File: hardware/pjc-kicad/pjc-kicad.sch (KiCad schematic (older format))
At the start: 90 parts

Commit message: More work on Hardware section of Developers Guide.
Also added 1k resistor and 100nF cap to USB Enable P-MOSFET to more closely match circuit in FT23R datasheet.
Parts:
- added C?: 100nF, symbol C
- added R?: 1k, symbol R
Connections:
- net +5V_USB: now also C?.2
- net ~USB_PWREN: now also C?.1, R?.2; no longer R?.2, U?.14 (CBUS3)
- new net: R?.1, R?.2, U?.14 (CBUS3)
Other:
- moved on the sheet: C?, CON?, L?, Q?, R?, TP?, U?

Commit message: Finished Hardware section in Dev Guide
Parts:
- gave numbers to parts that had none: 90
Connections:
- net GND: now also U10.1 (S), U8.4 (S); no longer U10.4 (S), U8.1 (S)
- net LAMP_EN: now also TP16.1, U10.5 (G); no longer R16.1, TP12.1, U8.2 (G)
- net LED_EN_GREEN: now also U10.2 (G); no longer U10.5 (G)
- net LED_EN_RED: now also R16.1, TP12.1, U8.2 (G); no longer TP16.1, U10.5 (G)
- net LED_EN_YELLOW: now also U8.5 (G); no longer U8.2 (G)
- net at U5.6 ((PCINT20/XCK/T0)PD4): now also JP1.2, R15.1
- net at CON9.2 (PM): now also U10.6 (D); no longer U10.3 (D)
- net at CON7.2 (PM): now also U8.3 (D); no longer U8.6 (D)

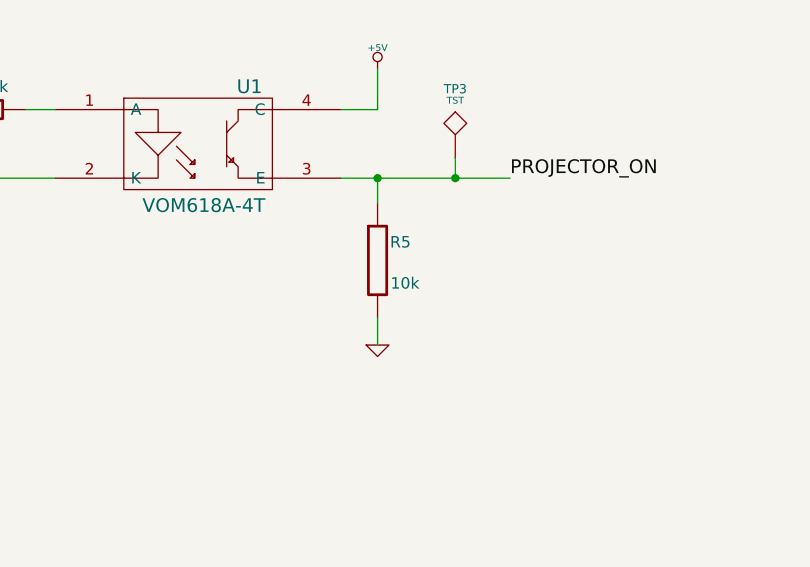
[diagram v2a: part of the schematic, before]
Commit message: More work on Firmware section of doc and put 20kOhm pulldown on opto collector to reduce the current needed to saturate it (useful for 3.3V inputs).
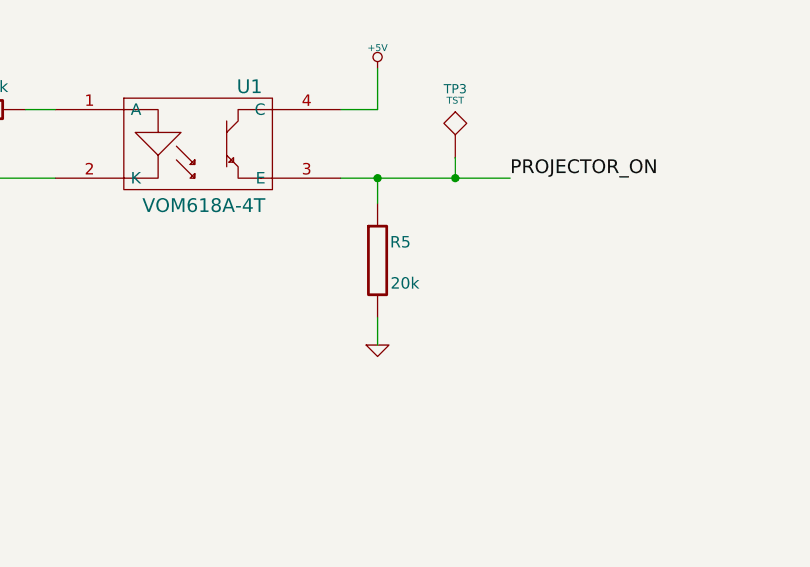
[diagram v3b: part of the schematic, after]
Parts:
- R5: value 10k -> 20k

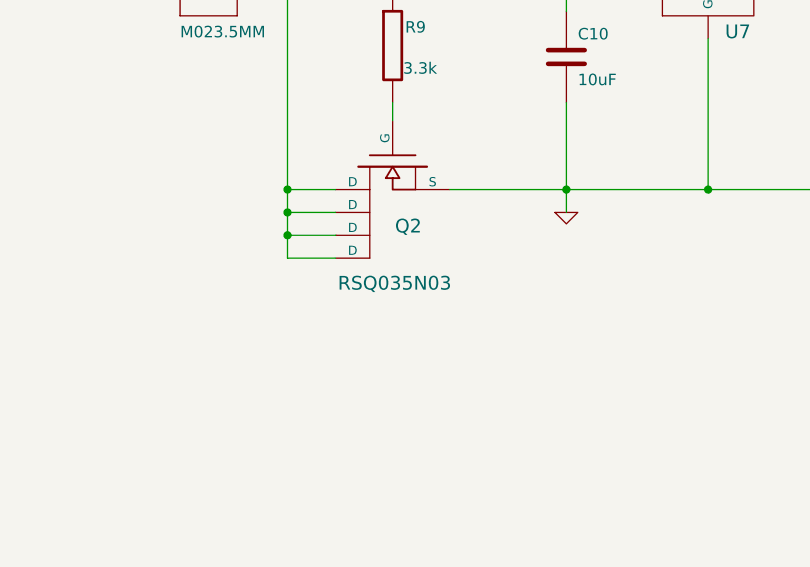
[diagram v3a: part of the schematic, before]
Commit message: Replace Rohm RSQ035N03 with RSQ045N03 since the former appears to be discontinued.  The latter has better specs anyway.
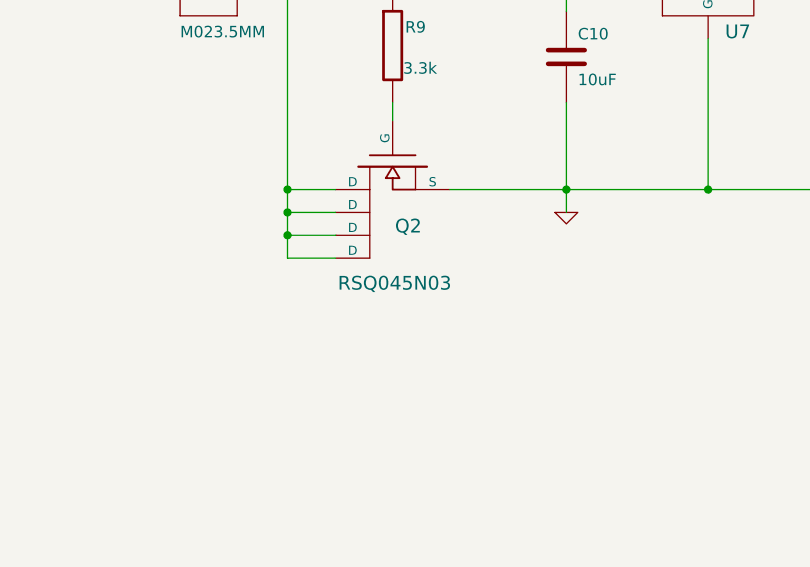
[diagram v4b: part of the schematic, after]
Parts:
- Q2: value RSQ035N03 -> RSQ045N03
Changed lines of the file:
@@
-EESchema Schematic File Version 2  date Wed 13 Feb 2013 07:00:38 PM EST
+EESchema Schematic File Version 2  date Sat 23 Feb 2013 07:02:45 PM EST
 LIBS:power
 LIBS:device
@@
 Sheet 1 1
 Title "Projector Controller Board"
-Date "13 feb 2013"
+Date "24 feb 2013"
 Rev "A"
 Comp ""
@@
 P 11090 3730
 F 0 "Q2" V 11350 3720 60  0000 R CNN
-F 1 "RSQ035N03" V 11600 3970 60  0000 R CNN
+F 1 "RSQ045N03" V 11600 3970 60  0000 R CNN
 F 2 "" H 11090 3730 60  0001 C CNN
 F 3 "" H 11090 3730 60  0001 C CNN

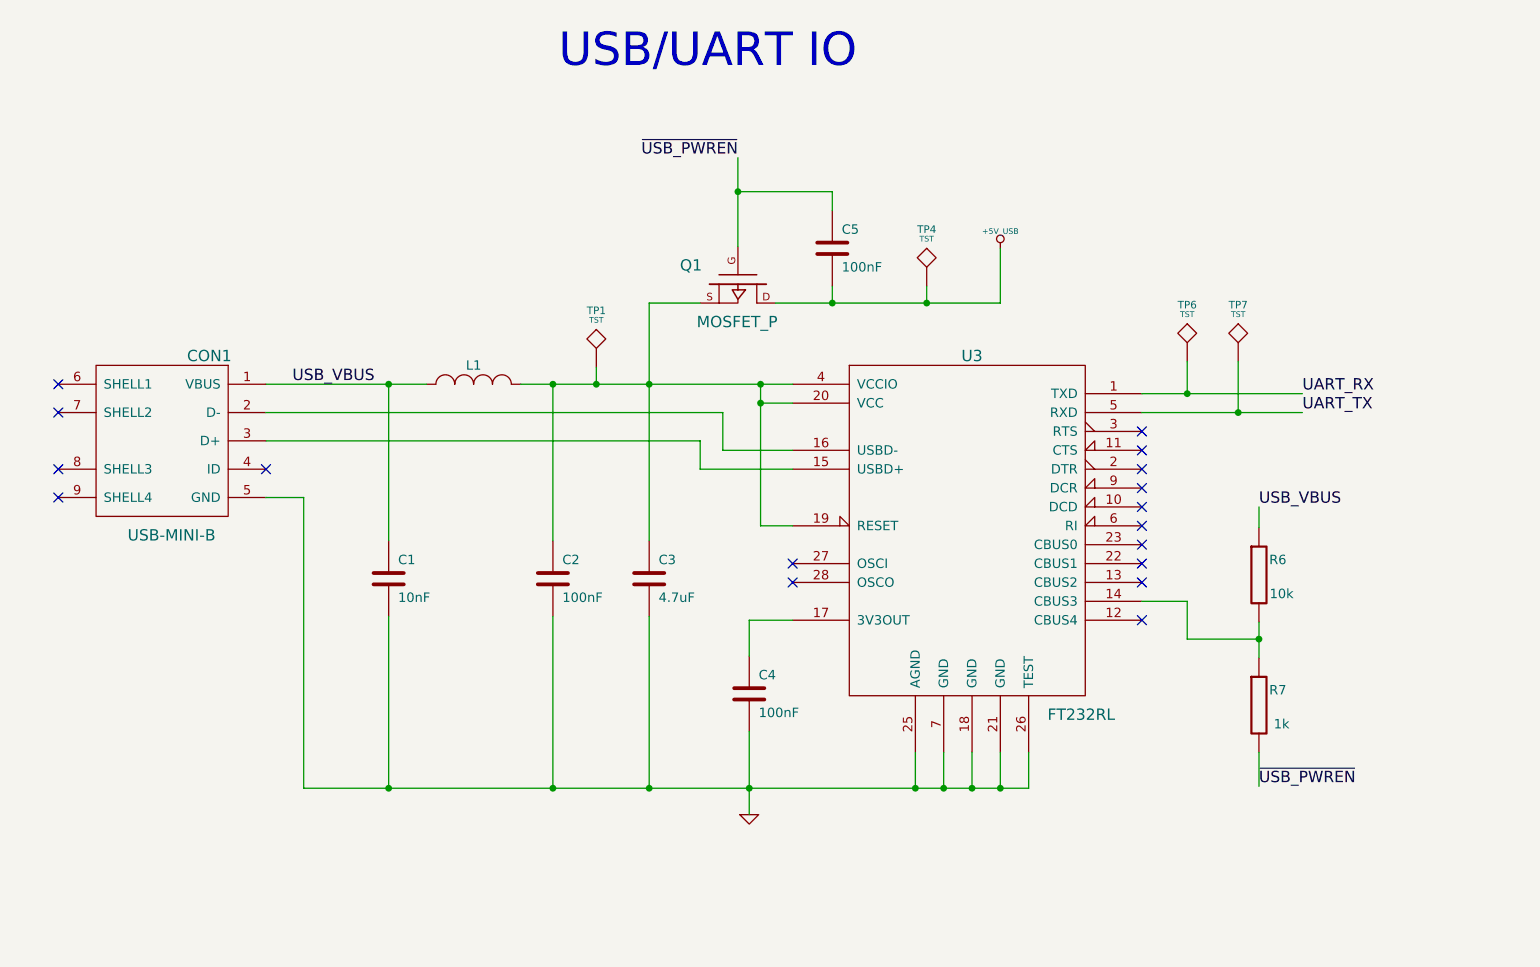
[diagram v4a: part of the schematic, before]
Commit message: Fix schematic errors found by KiCad and create symbol<-->footprint associations
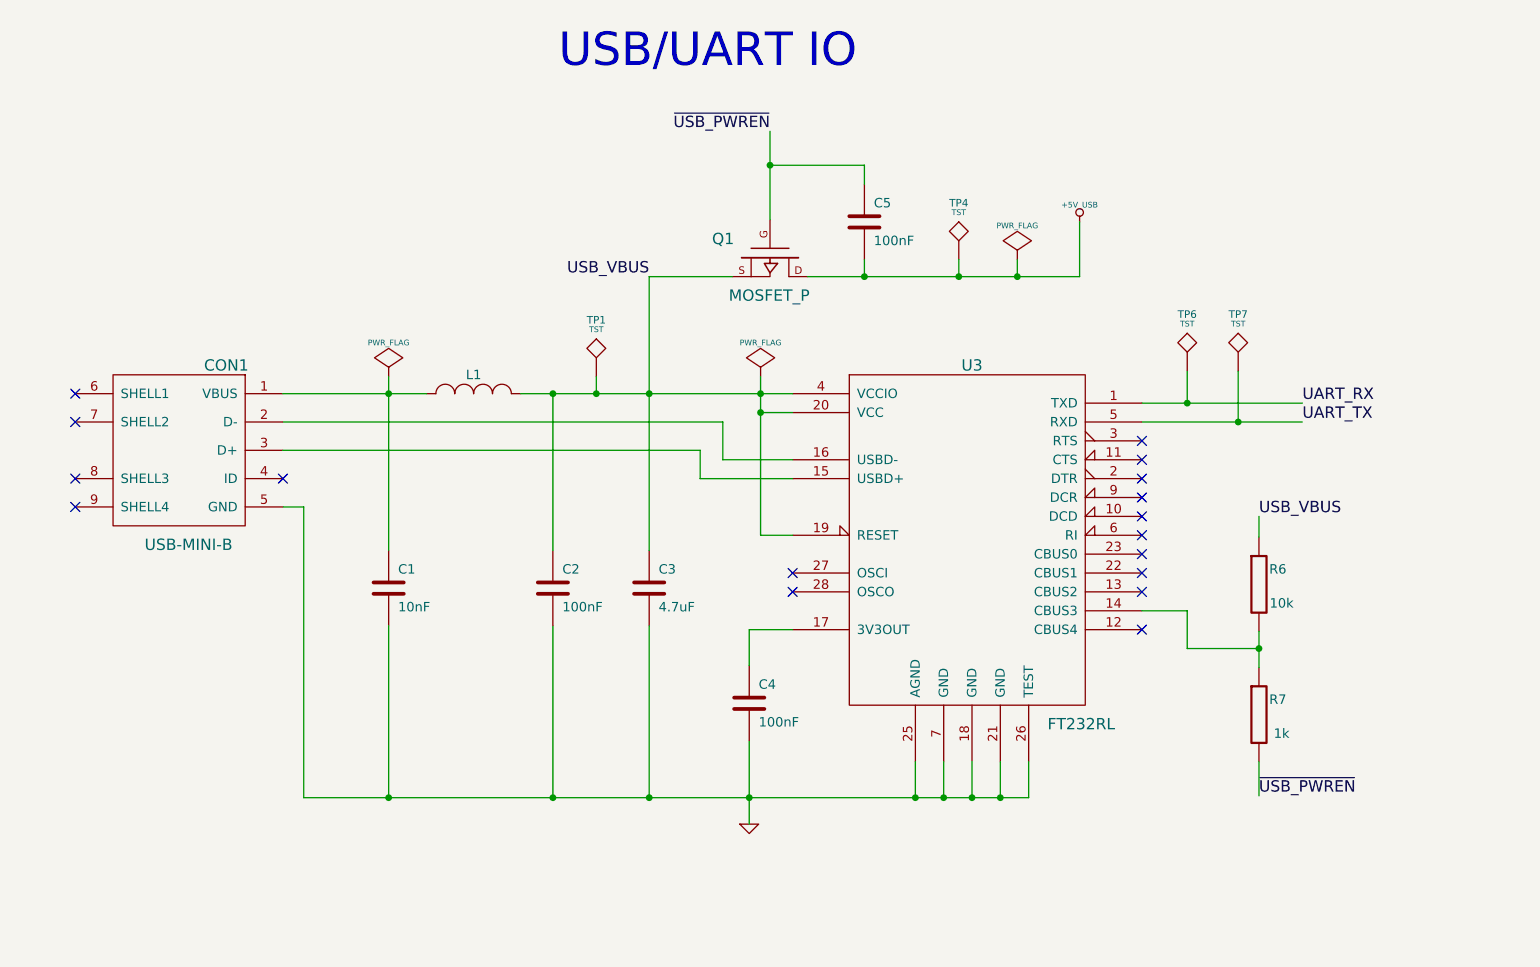
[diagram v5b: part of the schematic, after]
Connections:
- net USB_VBUS: now also C2.1, C3.1, L1.2, Q1.S, TP1.1, U3.19 (RESET), U3.20 (VCC), U3.4 (VCCIO); no longer C1.1, CON1.1 (VBUS), L1.1
- new net: C1.1, CON1.1 (VBUS), L1.1
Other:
- moved on the sheet: C1, C2, C3, C4, C5, CON1, L1, Q1, R6, R7, TP1, TP4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

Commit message: Began laying out board
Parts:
- removed TP6, TP7: TST, symbol TST

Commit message: More work on layout
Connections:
- net LAMP_EN: now also R16.1
- net LED_EN_RED: no longer R16.1
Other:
- moved on the sheet: R16

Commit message: Changed crystal oscillator caps to 33pF
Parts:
- C12, C13: value 22pF -> 33pF
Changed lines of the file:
@@
-EESchema Schematic File Version 2  date Tue 26 Feb 2013 09:13:41 PM EST
+EESchema Schematic File Version 2  date Sun 03 Mar 2013 10:54:55 PM EST
 LIBS:power
 LIBS:device
@@
 Sheet 1 1
 Title "Projector Controller Board"
-Date "26 feb 2013"
+Date "4 mar 2013"
 Rev "A"
 Comp ""
@@
 P 14410 7820
 F 0 "C13" V 14570 7780 50  0000 L CNN
-F 1 "22pF" V 14250 7720 50  0000 L CNN
+F 1 "33pF" V 14250 7720 50  0000 L CNN
 F 2 "" H 14410 7820 60  0001 C CNN
 F 3 "" H 14410 7820 60  0001 C CNN
@@
 P 14410 7220
 F 0 "C12" V 14570 7180 50  0000 L CNN
-F 1 "22pF" V 14250 7120 50  0000 L CNN
+F 1 "33pF" V 14250 7120 50  0000 L CNN
 F 2 "" H 14410 7220 60  0001 C CNN
 F 3 "" H 14410 7220 60  0001 C CNN
